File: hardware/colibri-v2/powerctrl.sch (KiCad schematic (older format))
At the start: 33 parts

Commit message: Work on power conrol sheet
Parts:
- removed C?: 33nF, Capacitors_SMD:C_0805, symbol C
- removed C?: 1uF, Capacitors_SMD:C_0805, symbol C
- removed C? (x2): 100nF, Capacitors_SMD:C_0805, symbol C
- removed R?: 1K, Resistors_SMD:R_0603, symbol R
- removed R?: 10K, Resistors_SMD:R_0603, symbol R
- removed R?: 100K, Resistors_SMD:R_0603, symbol R
- removed SW?: SW_PUSH, symbol SW_PUSH
- removed SW?: OS102011MA1QN1, symbol OS102011MA1QN1
- removed U?: LTC2954CTS8-2, symbol LTC2954CTS8-2
- added R? (x2): 100R/5%, Resistors_SMD:R_0603, symbol R_SMT
- added SW?: ALPS-SPPJ320600, symbol ALPS-SPPJ320600
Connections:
- wire segments 94 -> 105
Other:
- moved on the sheet: CON?, D?, Q?, R?

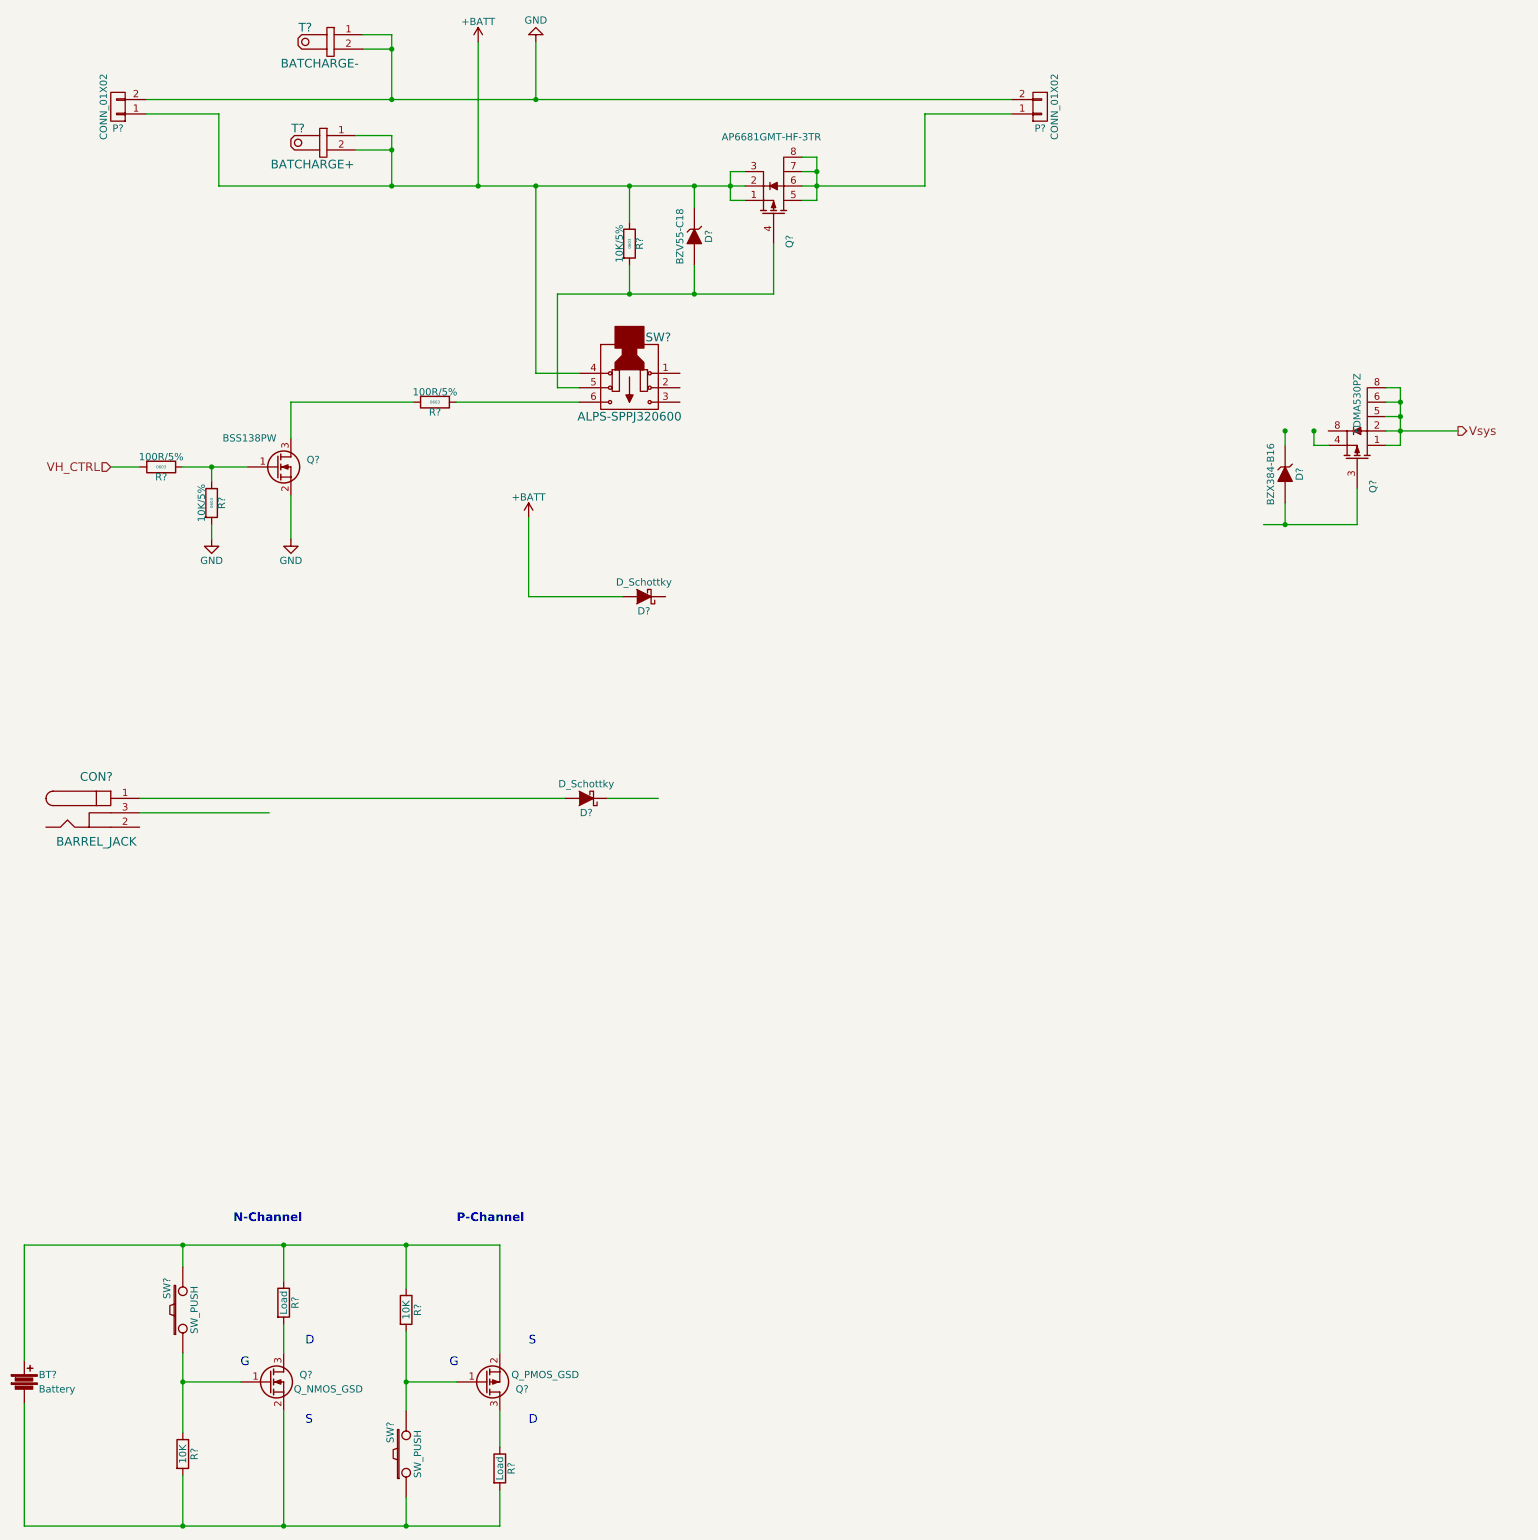
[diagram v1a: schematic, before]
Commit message: Work on power conrol sheet
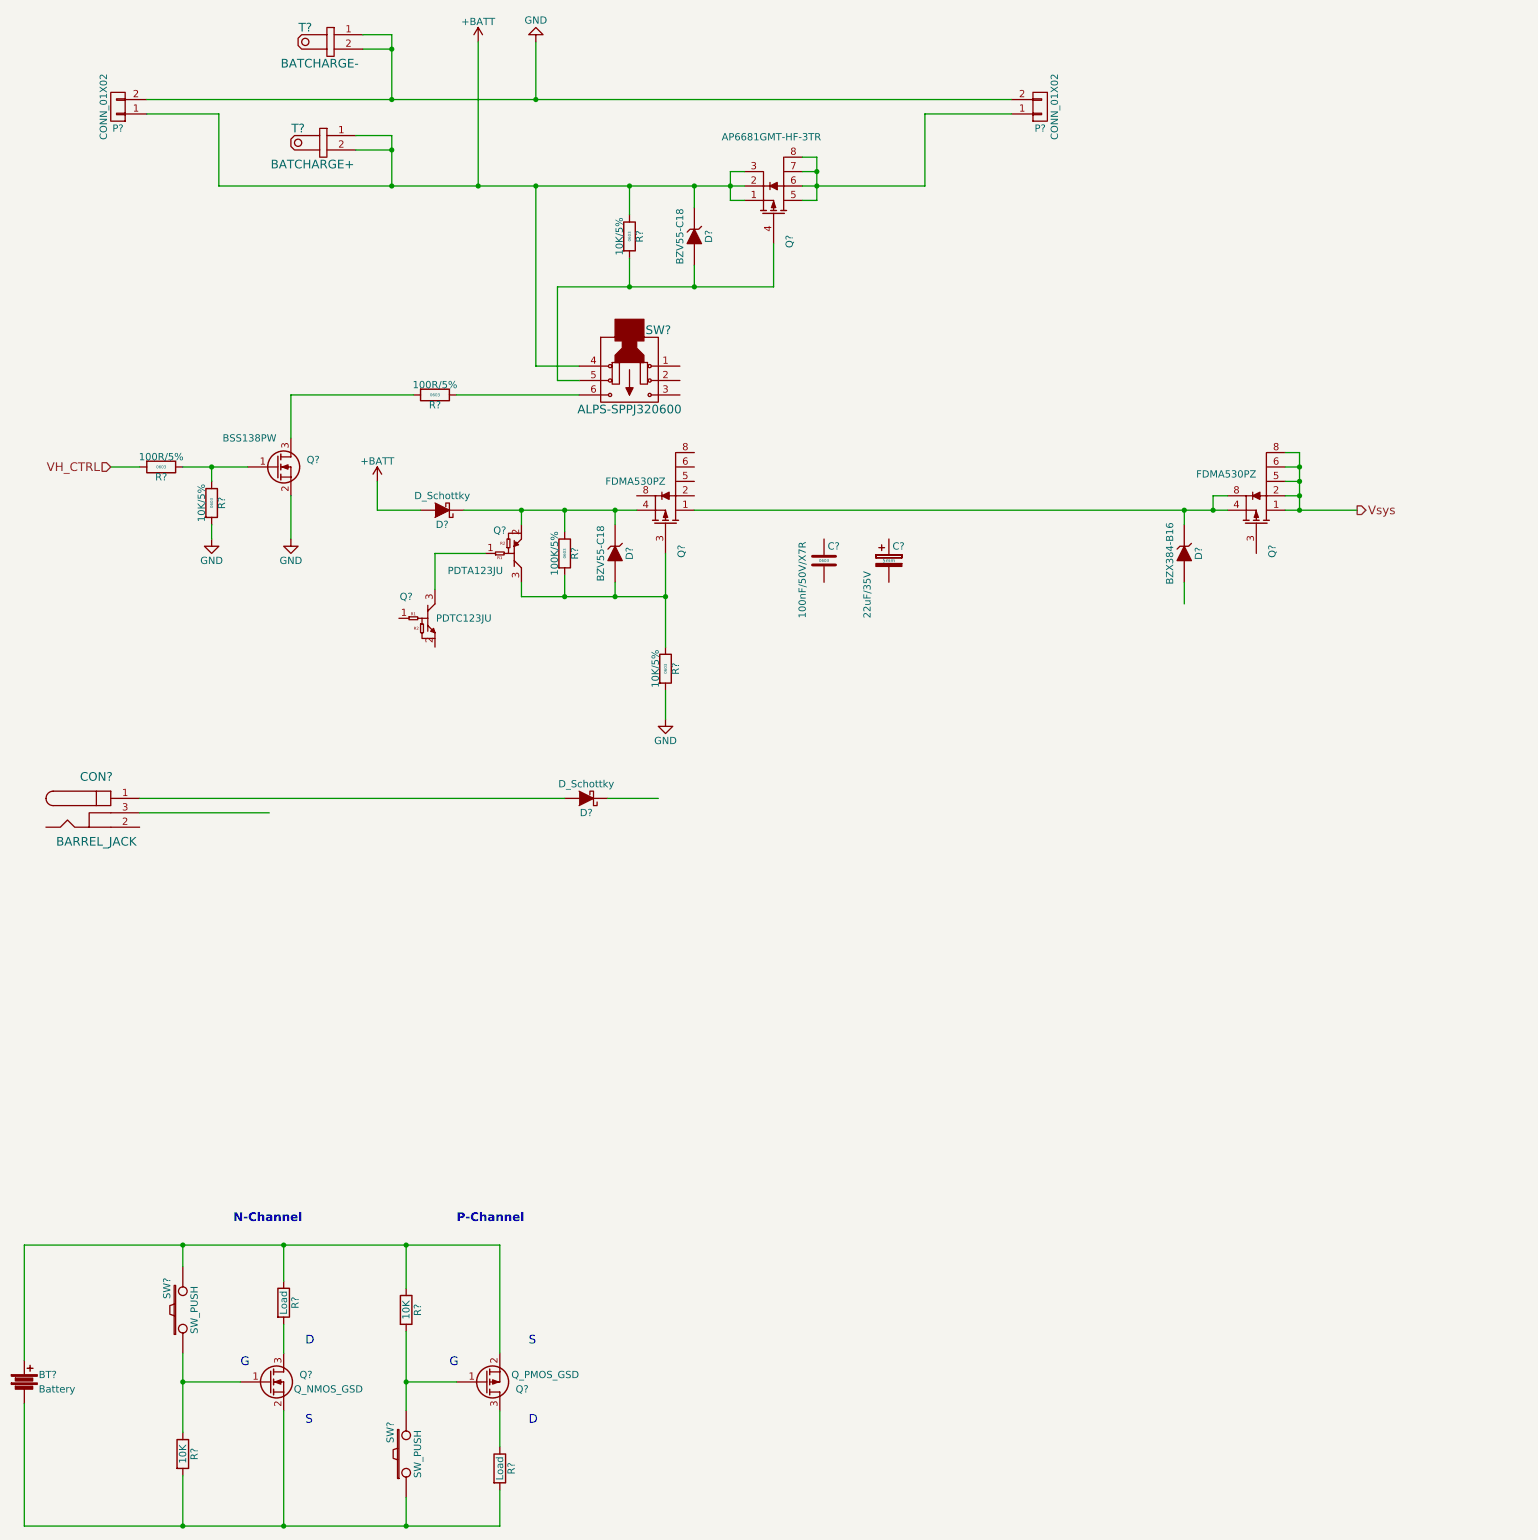
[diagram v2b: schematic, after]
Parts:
- added C?: 100nF/50V/X7R, Capacitors_SMD:C_0603, symbol C_SMT
- added C?: 22uF/35V, Capacitors_SMD:c_elec_5x5.7, symbol CP_SMT
- added D?: BZV55-C18, symbol ZENER
- added Q?: PDTA123JU, TO_SOT_Packages_SMD:SOT-323, symbol RET_PNP_SMT
- added Q?: PDTC123JU, TO_SOT_Packages_SMD:SOT-323, symbol RET_NPN_SMT
- added Q?: FDMA530PZ, symbol FDMA530PZ
- added R?: 10K/5%, Resistors_SMD:R_0603, symbol R_SMT
- added R?: 100K/5%, Resistors_SMD:R_0603, symbol R_SMT
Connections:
- wire segments 105 -> 86
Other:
- moved on the sheet: D?, Q?, R?, SW?

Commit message: Work on power control sheet
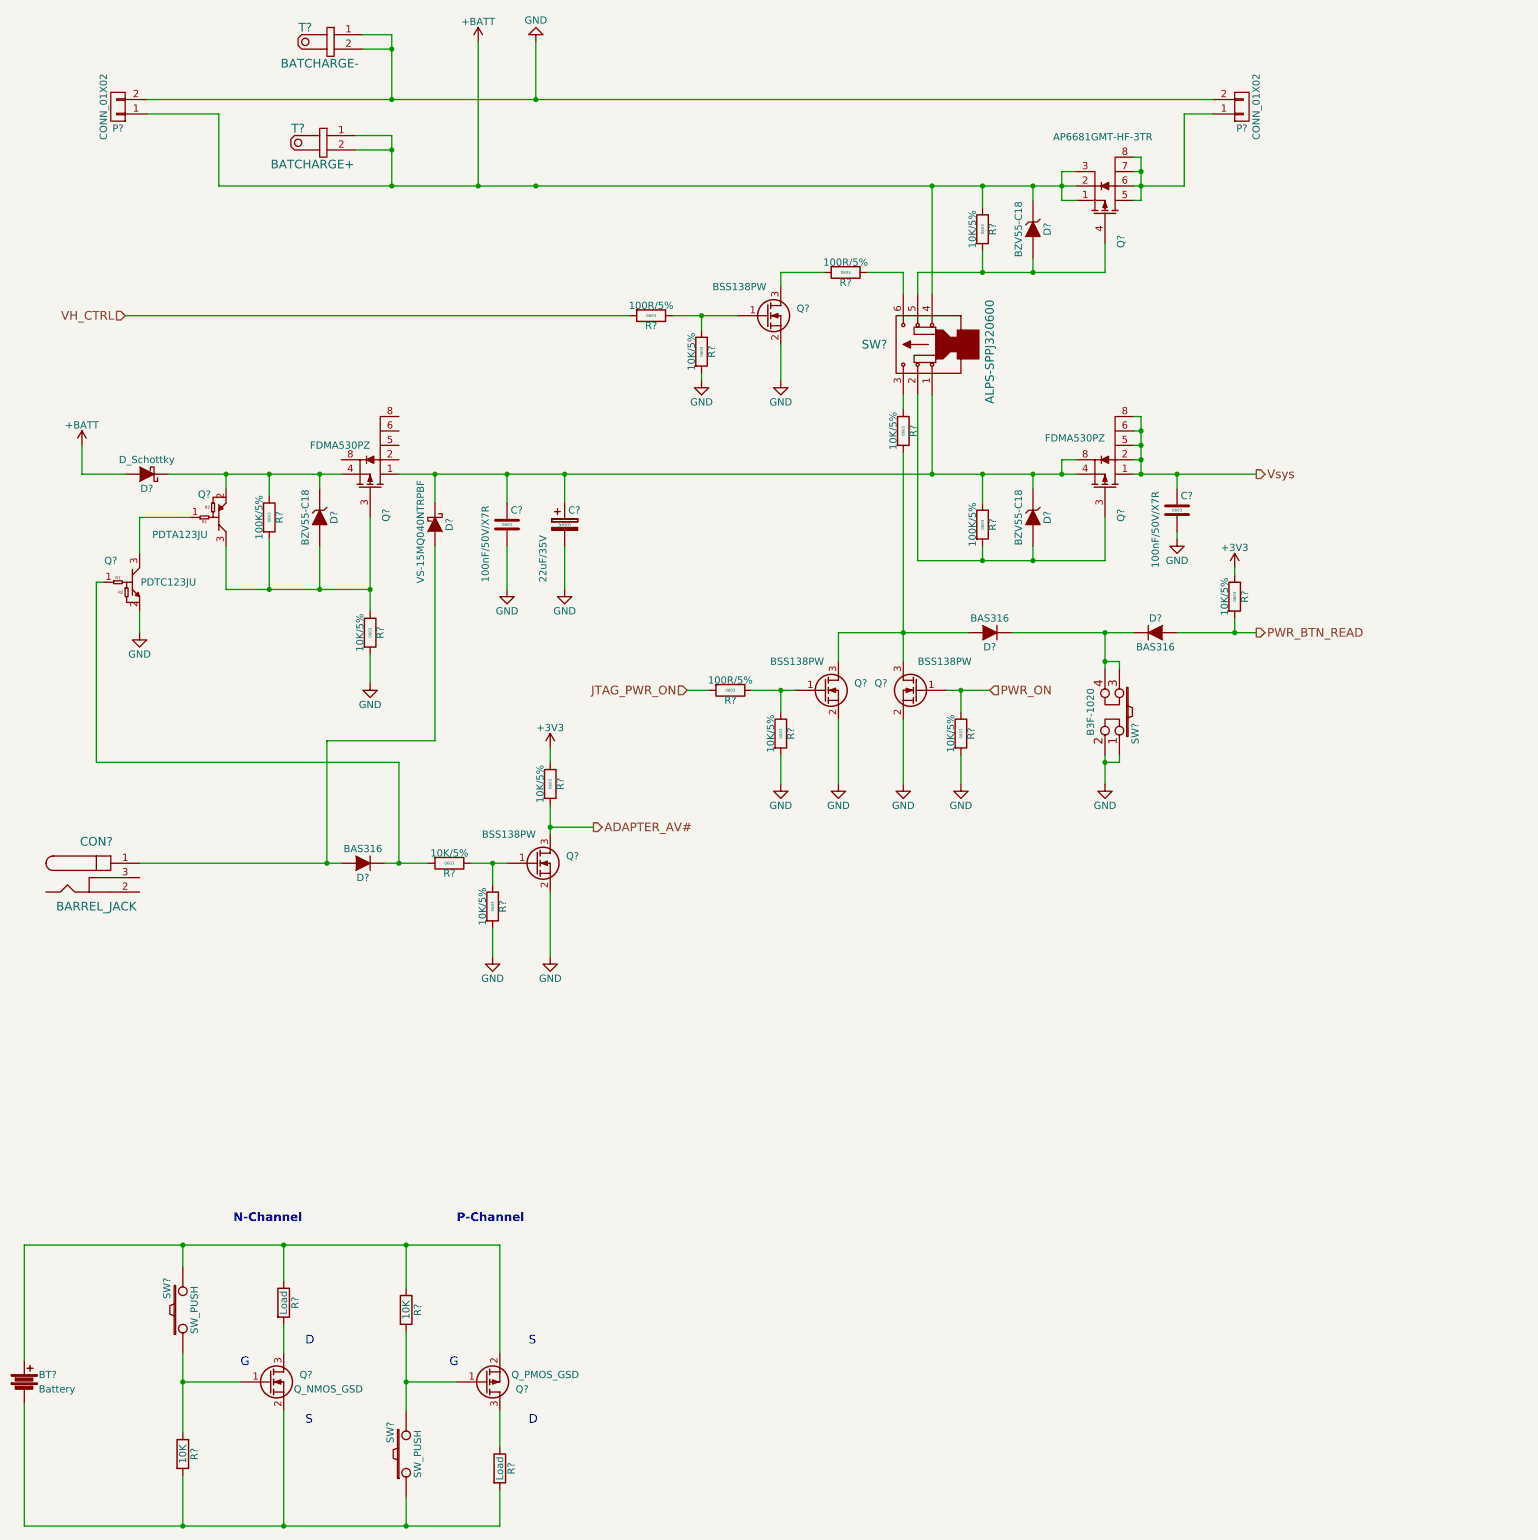
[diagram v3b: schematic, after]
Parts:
- added C?: 100nF/50V/X7R, Capacitors_SMD:C_0603, symbol C_SMT
- added D? (x3): BAS316, symbol D
- added Q? (x3): BSS138PW, symbol Q_NMOS_GSD
- added R?: 100K/5%, Resistors_SMD:R_0603, symbol R_SMT
- added R? (x7): 10K/5%, Resistors_SMD:R_0603, symbol R_SMT
- added R?: 100R/5%, Resistors_SMD:R_0603, symbol R_SMT
- added SW?: B3F-1020, symbol SW_PUSH_TACKTILE
- D?: value D_Schottky -> VS-15MQ040NTRPBF; Part (none) -> 1463215; Provider (none) -> Farnell; SMT (none) -> na
- D?: value BZX384-B16 -> BZV55-C18; Part (none) -> 1097211; Provider (none) -> Farnell; SMT (none) -> na
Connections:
- net labels added: +3V3, ADAPTER_AV#, JTAG_PWR_ON, PWR_BTN_READ, PWR_ON
- wire segments 86 -> 135
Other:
- moved on the sheet: C?, CON?, D?, P?, Q?, R?, SW?

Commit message: work on power control
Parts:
- removed BT?: Battery, symbol Battery
- removed Q?: Q_NMOS_GSD, symbol Q_NMOS_GSD
- removed Q?: Q_PMOS_GSD, symbol Q_PMOS_GSD
- removed R? (x2): Load, Resistors_SMD:R_0603, symbol R
- removed R? (x2): 10K, Resistors_SMD:R_0603, symbol R
- removed SW? (x2): SW_PUSH, symbol SW_PUSH
- added C?: 100nF/50V/X7R, Capacitors_SMD:C_0603, symbol C_SMT
- added DL?: RED, LEDs:LED-0603, symbol LED_SMT
- added Q?: PDTA123JU, TO_SOT_Packages_SMD:SOT-323, symbol RET_PNP_SMT
- added Q?: PDTC123JU, TO_SOT_Packages_SMD:SOT-323, symbol RET_NPN_SMT
- added R?: 2k2/5%, Resistors_SMD:R_0603, symbol R_SMT
- added R?: 100K/5%, Resistors_SMD:R_0603, symbol R_SMT
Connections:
- net +3V3: now also Q?.1
- net +BATT: now also Q?.2
- net GND: now also CON?.2, CON?.3, C?.2, DL?.1 (K), Q?.2, R?.2
- net at D?.1 (K), D?.1 (K), Q?.2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: now also Q?.8 (S)
- net at C?.1, C?.1, D?.1 (K)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: now also Q?.2 (D), Q?.5 (D), Q?.6 (D), Q?.8 (S)
- net at CON?.1, D?.2 (A), D?.2 (A): now also R?.1
- new net: DL?.2 (A), R?.2
- new net: Q?.1, Q?.3
- new net BAT_MSRMNT: C?.1, Q?.3, R?.1
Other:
- note added: "10 OR 100?"
- note added: "100K or 10K?"
- note added: "Better to\nuse MSRMNT_ON"
- note added: "What is this for?"
- note removed: "D"
- note removed: "G"
- note removed: "N-Channel"
- note removed: "P-Channel"
- note removed: "S"
- moved on the sheet: C?, CON?, D?, P?, Q?, R?, SW?, T?
